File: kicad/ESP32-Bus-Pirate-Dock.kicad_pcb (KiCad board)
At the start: 4 copper layers, 80 x 73.8 mm, 34 parts, among them CN1 HX25418-10WA, J1 Conn_01x10V, J2 Conn_01x22, J3 Conn_01x22, J4 Conn_02x03, J5 Conn_01x22, J6 Conn_01x22, J7 Conn_01x22, Q1 2N7002, U2 LDL1117S33R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

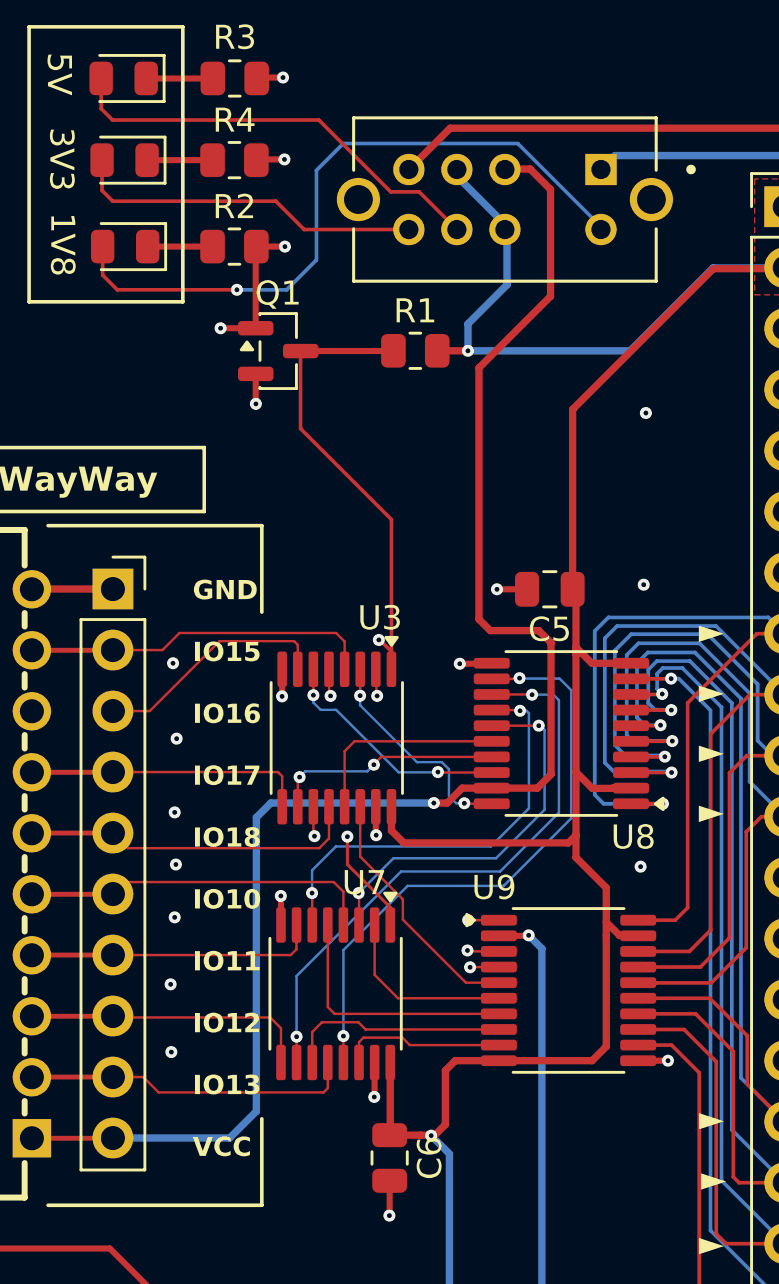
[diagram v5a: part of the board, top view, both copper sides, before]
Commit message: Updated PCB to include TXS disabling
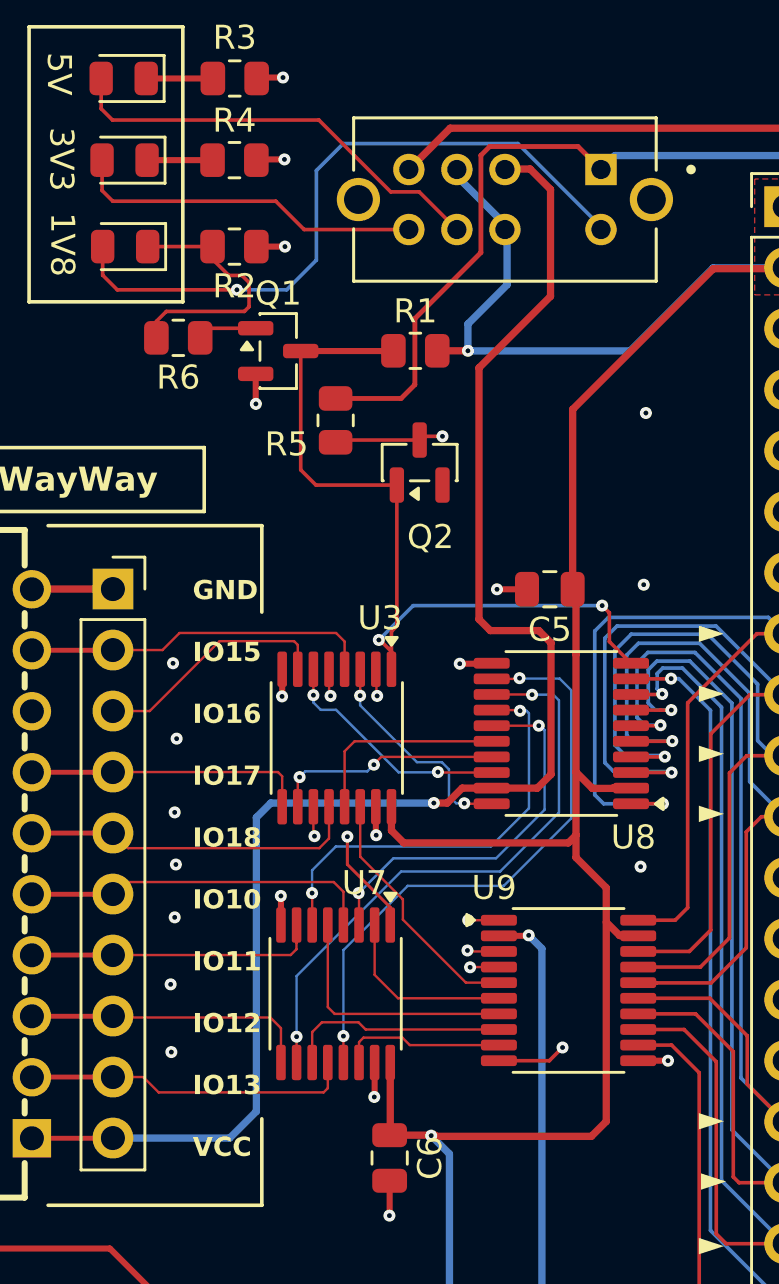
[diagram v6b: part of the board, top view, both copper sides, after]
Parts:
- added Q2: 2N7002, Package_TO_SOT_SMD:SOT-23, F.Cu at (151.8, 81.1)
- added R5: 100k, Resistor_SMD:R_0805_2012Metric, F.Cu at (148.3, 79.3)
- added R6: 100k, Resistor_SMD:R_0805_2012Metric, F.Cu at (141.8, 75.9)
- turned R2 to 180 degrees
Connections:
- Q1 pad 1: GND -> /Voltage Level Translator/GATE
- R2 pad 1: /Voltage Level Translator/D1_K -> GND
- R2 pad 2: GND -> /Voltage Level Translator/D1_K
- U8 pad 10: +3.3V -> /Voltage Level Translator/SEL
- U9 pad 10: +3.3V -> /Voltage Level Translator/OE2
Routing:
- net /Voltage Level Translator/OE2: track 0.00 -> 35.4 mm, vias 0 -> 2
- net +1V8: track 119.8 -> 139.6 mm
- net /Voltage Level Translator/SEL: track 35.9 -> 50.9 mm, vias 2 -> 3
- net /Voltage Level Translator/D1_K: track 2.70 -> 11.0 mm
- net GND: track 35.6 -> 30.7 mm, vias 30 -> 29
- net /Voltage Level Translator/GATE: track 0.00 -> 2.48 mm
- net +3.3V: track 120.2 -> 118.2 mm

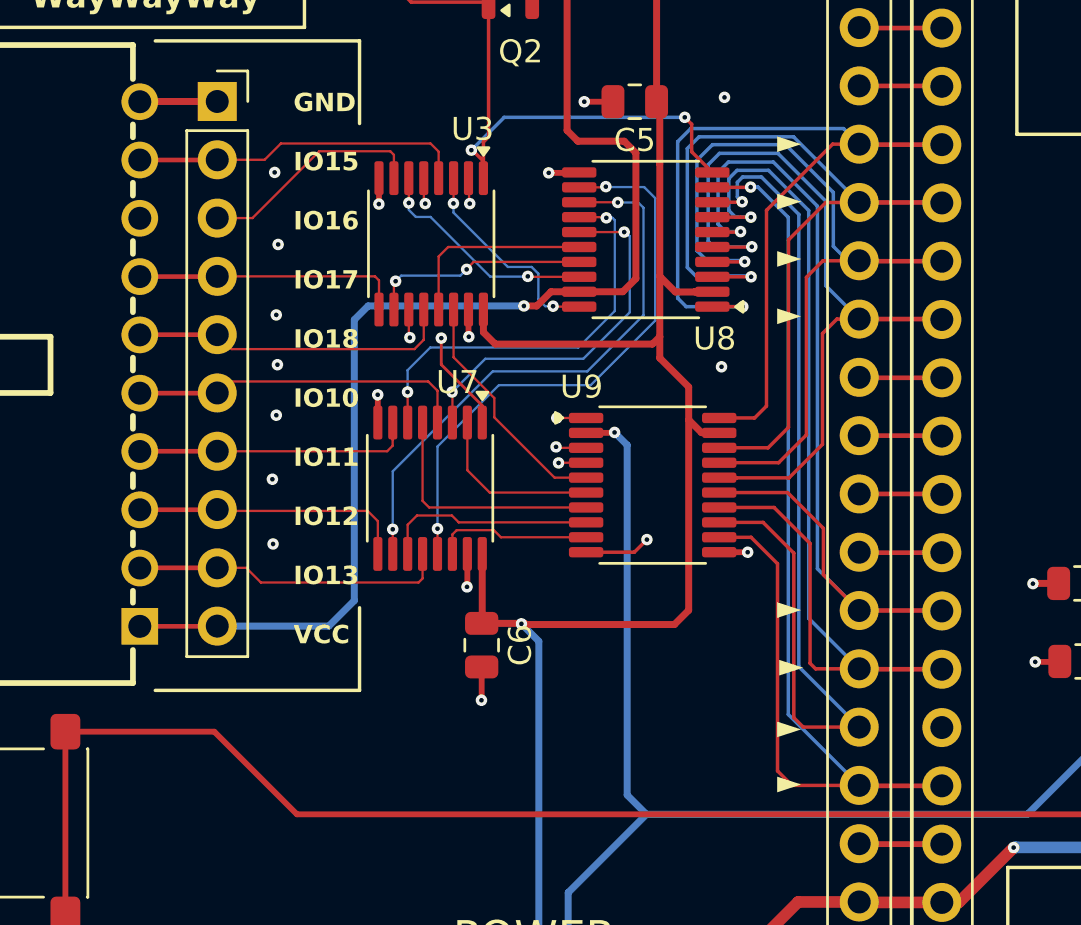
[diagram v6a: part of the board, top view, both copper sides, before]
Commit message: Added DRC
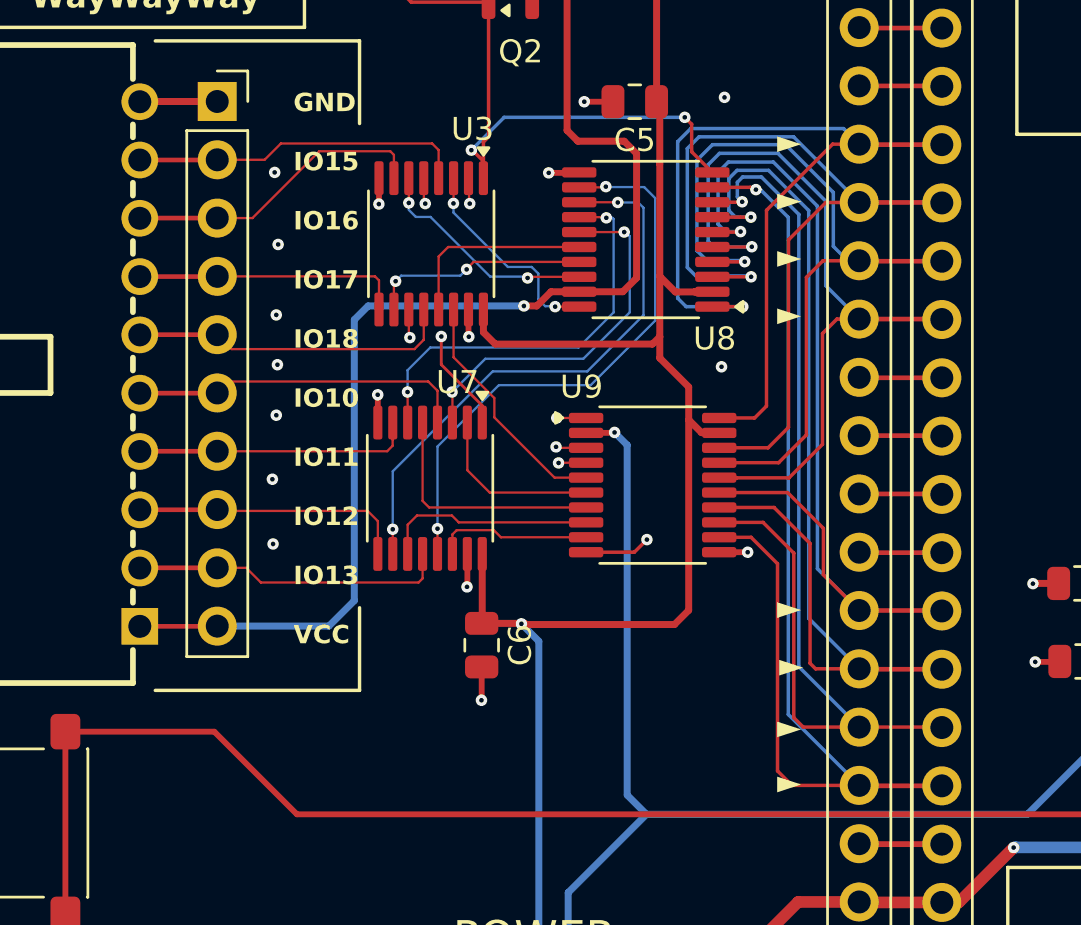
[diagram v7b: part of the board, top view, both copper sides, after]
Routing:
- net GPIO12: track 43.0 -> 46.6 mm
- net IO16: track 9.98 -> 13.4 mm

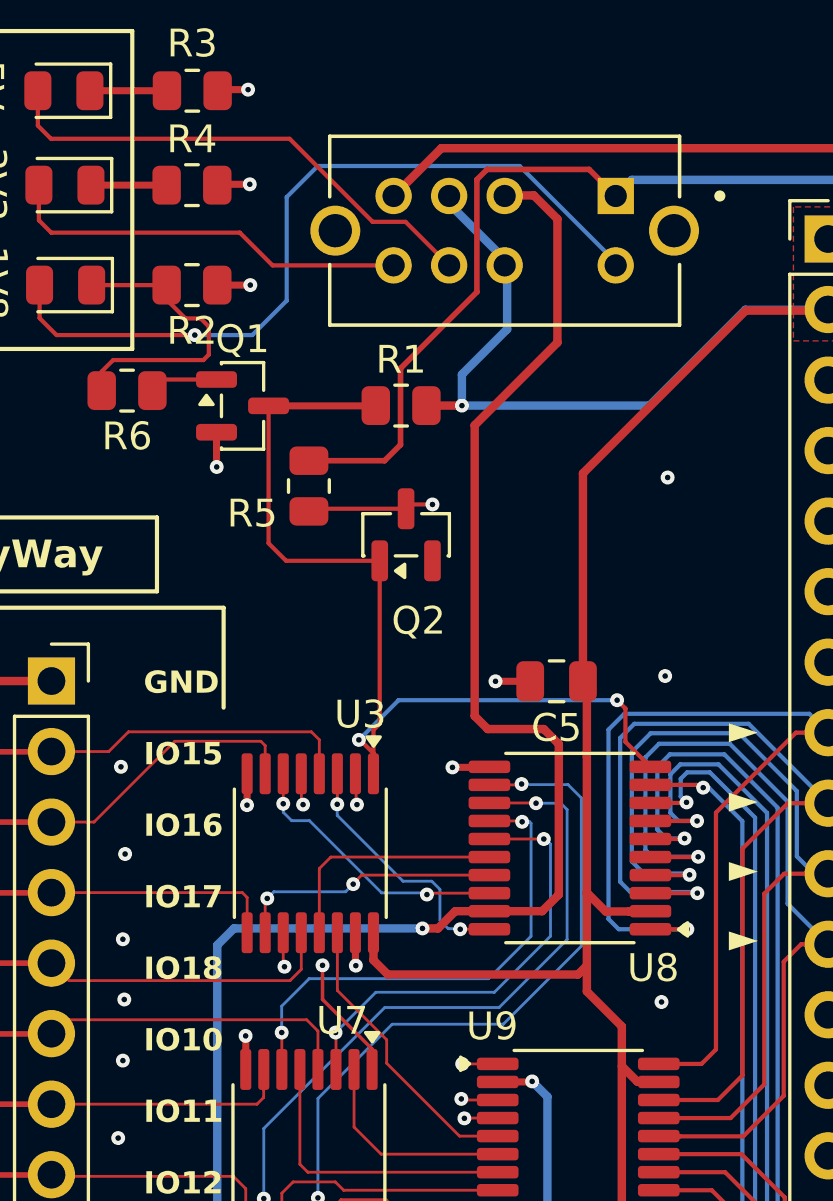
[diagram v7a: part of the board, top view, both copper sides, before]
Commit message: Reduced Logic circuit
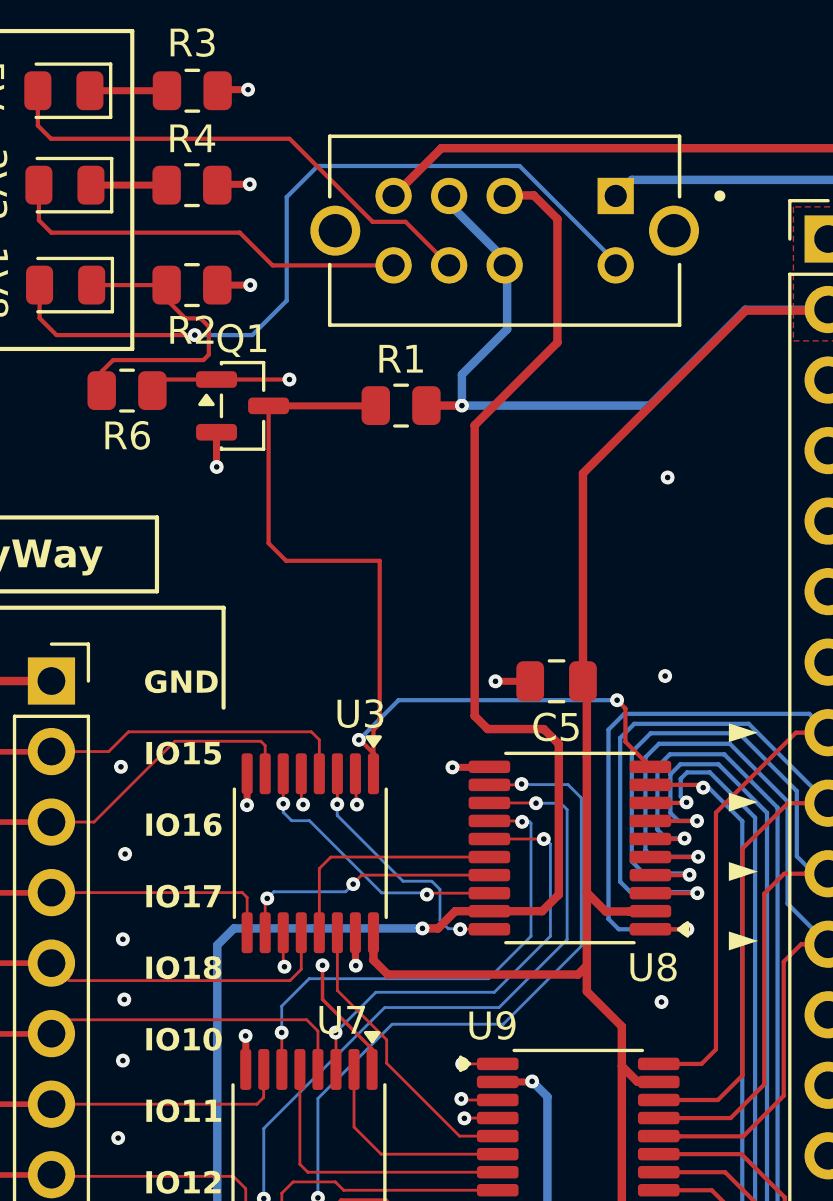
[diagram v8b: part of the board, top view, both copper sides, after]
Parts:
- removed Q2: 2N7002, Package_TO_SOT_SMD:SOT-23
- removed R5: 100k, Resistor_SMD:R_0805_2012Metric
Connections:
- U9 pad 10: /Voltage Level Translator/OE2 -> /Voltage Level Translator/GATE
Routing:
- net /Voltage Level Translator/GATE: track 2.48 -> 42.9 mm, vias 0 -> 2
- net /Voltage Level Translator/OE2: track 35.4 -> 0.00 mm, vias 2 -> 0
- net +1V8: track 139.6 -> 119.8 mm
